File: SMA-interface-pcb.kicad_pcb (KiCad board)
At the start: 2 copper layers, 19 x 60 mm, 9 parts, among them J1 Conn_Coaxial, J3 Conn_01x02_Pin, J4 USB_A_Stacked, J5 Conn_01x02_Pin, Q1 AO3400A, U1 EL817

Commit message: updated schematic to v0
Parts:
- added D2: D_Schottky, Diode_SMD:D_3220_8050Metric_Pad2.65x5.15mm_HandSolder, F.Cu at (131.0, 100.3)
- added F2: Polyfuse, Fuse:fuse, F.Cu at (123.0, 85.5)
- added J2: Conn_Coaxial, Connector_Coaxial:SMA_Amphenol_901-143_Horizontal, F.Cu at (68.5, 63.5)
- added J6: Conn_Coaxial, Connector_Coaxial:SMA_Amphenol_901-143_Horizontal, F.Cu at (102.0, 63.5)
- added J7: Conn_Coaxial, Connector_Coaxial:SMA_Amphenol_901-143_Horizontal, F.Cu at (118.0, 63.5)
- added J8: USB_A_Stacked, Connector_USB:USB_A_Wuerth_61400826021_Horizontal_Stacked, F.Cu at (117.6, 120.0)
- added Q2: AO3400A, Package_TO_SOT_SMD:SOT-23, F.Cu at (74.0, 130.2)
- added Q3: AO3400A, Package_TO_SOT_SMD:SOT-23, F.Cu at (125.0, 142.0)
- added Q4: AO3400A, Package_TO_SOT_SMD:SOT-23, F.Cu at (73.9, 118.0)
- added Q5: AO3400A, Package_TO_SOT_SMD:SOT-23, F.Cu at (103.5, 143.5)
- added Q6: AO3400A, Package_TO_SOT_SMD:SOT-23, F.Cu at (124.5, 131.4)
- added Q7: AO3400A, Package_TO_SOT_SMD:SOT-23, F.Cu at (74.5, 143.5)
- added Q8: AO3400A, Package_TO_SOT_SMD:SOT-23, F.Cu at (73.9, 104.2)
- added R10: 10k, Resistor_THT:R_Axial_DIN0207_L6.3mm_D2.5mm_P2.54mm_Vertical, F.Cu at (65.5, 129.0)
- added R11: 100, Resistor_THT:R_Axial_DIN0207_L6.3mm_D2.5mm_P2.54mm_Vertical, F.Cu at (57.7, 119.1)
- added R12: 10k, Resistor_THT:R_Axial_DIN0207_L6.3mm_D2.5mm_P2.54mm_Vertical, F.Cu at (65.5, 117.0)
- added R13: 100, Resistor_THT:R_Axial_DIN0207_L6.3mm_D2.5mm_P2.54mm_Vertical, F.Cu at (95.0, 134.0)
- added R14: 10k, Resistor_THT:R_Axial_DIN0207_L6.3mm_D2.5mm_P2.54mm_Vertical, F.Cu at (95.0, 142.0)
- added R15: 100, Resistor_THT:R_Axial_DIN0207_L6.3mm_D2.5mm_P2.54mm_Vertical, F.Cu at (116.5, 130.5)
- added R16: 10k, Resistor_THT:R_Axial_DIN0207_L6.3mm_D2.5mm_P2.54mm_Vertical, F.Cu at (133.0, 132.5)
- added R17: 100, Resistor_THT:R_Axial_DIN0207_L6.3mm_D2.5mm_P2.54mm_Vertical, F.Cu at (57.9, 145.1)
- added R18: 10k, Resistor_THT:R_Axial_DIN0207_L6.3mm_D2.5mm_P2.54mm_Vertical, F.Cu at (66.0, 143.0)
- added R19: 100, Resistor_THT:R_Axial_DIN0207_L6.3mm_D2.5mm_P2.54mm_Vertical, F.Cu at (57.5, 105.1)
- added R2: R, Resistor_THT:R_Axial_DIN0207_L6.3mm_D2.5mm_P2.54mm_Vertical, F.Cu at (84.0, 73.7)
- added R20: 10k, Resistor_THT:R_Axial_DIN0207_L6.3mm_D2.5mm_P2.54mm_Vertical, F.Cu at (65.5, 103.1)
- added R4: R, Resistor_THT:R_Axial_DIN0207_L6.3mm_D2.5mm_P2.54mm_Vertical, F.Cu at (101.0, 73.5)
- added R6: R, Resistor_THT:R_Axial_DIN0207_L6.3mm_D2.5mm_P2.54mm_Vertical, F.Cu at (117.6, 72.9)
- added R7: 100, Resistor_THT:R_Axial_DIN0207_L6.3mm_D2.5mm_P2.54mm_Vertical, F.Cu at (56.9, 131.2)
- added R8: 100, Resistor_THT:R_Axial_DIN0207_L6.3mm_D2.5mm_P2.54mm_Vertical, F.Cu at (116.5, 143.0)
- added R9: 10k, Resistor_THT:R_Axial_DIN0207_L6.3mm_D2.5mm_P2.54mm_Vertical, F.Cu at (133.0, 142.5)
- added RZ1: RP2040-Zero, RP2040:RP2040_Zero_Castellated, F.Cu at (96.5, 116.0)
- J1: footprint SMA:SMA_Amphenol_901-143_Horizontal -> Connector_Coaxial:SMA_Amphenol_901-143_Horizontal
- J3: footprint SMA:Molex_Mini-Fit_Jr_5569-02A2_2x01_P4.20mm_Horizontal -> Connector_Molex:Molex_Mini-Fit_Jr_5569-02A2_2x01_P4.20mm_Horizontal
- Q1: moved to F.Cu
- R1: value R -> 100; footprint SMA:R_tht1270_smd3216 -> Resistor_THT:R_Axial_DIN0207_L6.3mm_D2.5mm_P2.54mm_Vertical
- R3: value R -> 10k; footprint SMA:R_tht1270_smd3216 -> Resistor_THT:R_Axial_DIN0207_L6.3mm_D2.5mm_P2.54mm_Vertical
- R5: footprint SMA:R_tht1270_smd3216 -> Resistor_THT:R_Axial_DIN0207_L6.3mm_D2.5mm_P2.54mm_Vertical
- U1: value EL817 -> 74HC14; footprint Package_DIP:DIP-4_W7.62mm_SMDSocket_SmallPads -> Button_Switch_SMD:SW_DIP_SPSTx07_Slide_KingTek_DSHP07TJ_W5.25mm_P1.27mm_JPin; moved to F.Cu
- moved J4 64.0 mm to (72.1, 86.5), turned to -90 degrees
- moved R5 61.5 mm to (68.0, 74.0), turned to 180 degrees
- moved R1 60.6 mm to (89.0, 134.0)
- moved R3 54.4 mm to (89.0, 142.0), turned to -90 degrees
- moved J1 45.5 mm to (85.0, 63.5)
- moved Q1 44.7 mm to (103.4, 134.9), turned to 0 degrees
- moved U1 37.4 mm to (96.5, 92.5), turned to 0 degrees
- moved J5 25.8 mm to (131.5, 60.0), turned to 90 degrees
- moved J3 8.24 mm to (132.5, 82.3)
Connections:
- J1 pad 1: Net-(J1-In) -> /sma1
- J3 pad 1: GND -> /power input
- J3 pad 2: VCC -> /vcc
- J4 pad 1: VCC -> /vcc
- J4 pad 2: unconnected-(J4-D1--Pad2) -> /2illumination1-
- J4 pad 3: /illumination -> /2sound1+
- J4 pad 5: VCC -> /vcc
- J4 pad 6: unconnected-(J4-D2--Pad6) -> /2illumination2-
- J4 pad 7: /illumination -> /2sound2+
- J5 pad 1: GND -> /power input
- J5 pad 2: VCC -> /vcc
- Q1 pad 3: /illumination -> Net-(J8-D2-)
- R1 pad 1: Net-(R1-Pad1) -> /illumination
- R5 pad 1: Net-(J1-In) -> /sma3
- R5 pad 2: Net-(R5-Pad2) -> GND
- U1 pad 1: Net-(R5-Pad2) -> /sma1
- U1 pad 2: GND -> /SMA_con1
- U1 pad 3: Net-(R1-Pad1) -> /sma2
- U1 pad 4: VCC -> /SMA_con2
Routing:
- net /vcc: track 0.00 -> 149.7 mm, vias 0 -> 6
- net /2sound1+: track 0.00 -> 75.1 mm, vias 0 -> 2
- net VCC: track 65.2 -> 0.00 mm
- net /2sound2+: track 0.00 -> 56.6 mm, vias 0 -> 2
- net /sma3: track 0.00 -> 44.7 mm
- net /2illumination2-: track 0.00 -> 42.1 mm, vias 0 -> 2
- net /sma4: track 0.00 -> 40.2 mm
- net Net-(RZ1-GP10): track 0.00 -> 37.9 mm
- net /sound: track 0.00 -> 33.6 mm, vias 0 -> 2
- net /SMA_con4: track 0.00 -> 33.3 mm, vias 0 -> 2
- net Net-(J8-D1-): track 0.00 -> 33.0 mm, vias 0 -> 2
- net /sma2: track 0.00 -> 32.2 mm
- net /power input: track 0.00 -> 31.7 mm
- net Net-(R5-Pad2): track 30.3 -> 0.00 mm
- net /sound2: track 0.00 -> 30.2 mm
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- added copper zone on F.Cu, net GND
- removed copper zone on B.Cu, net GND
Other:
- board size 19 x 60 mm -> 15.6 x 20.9 mm

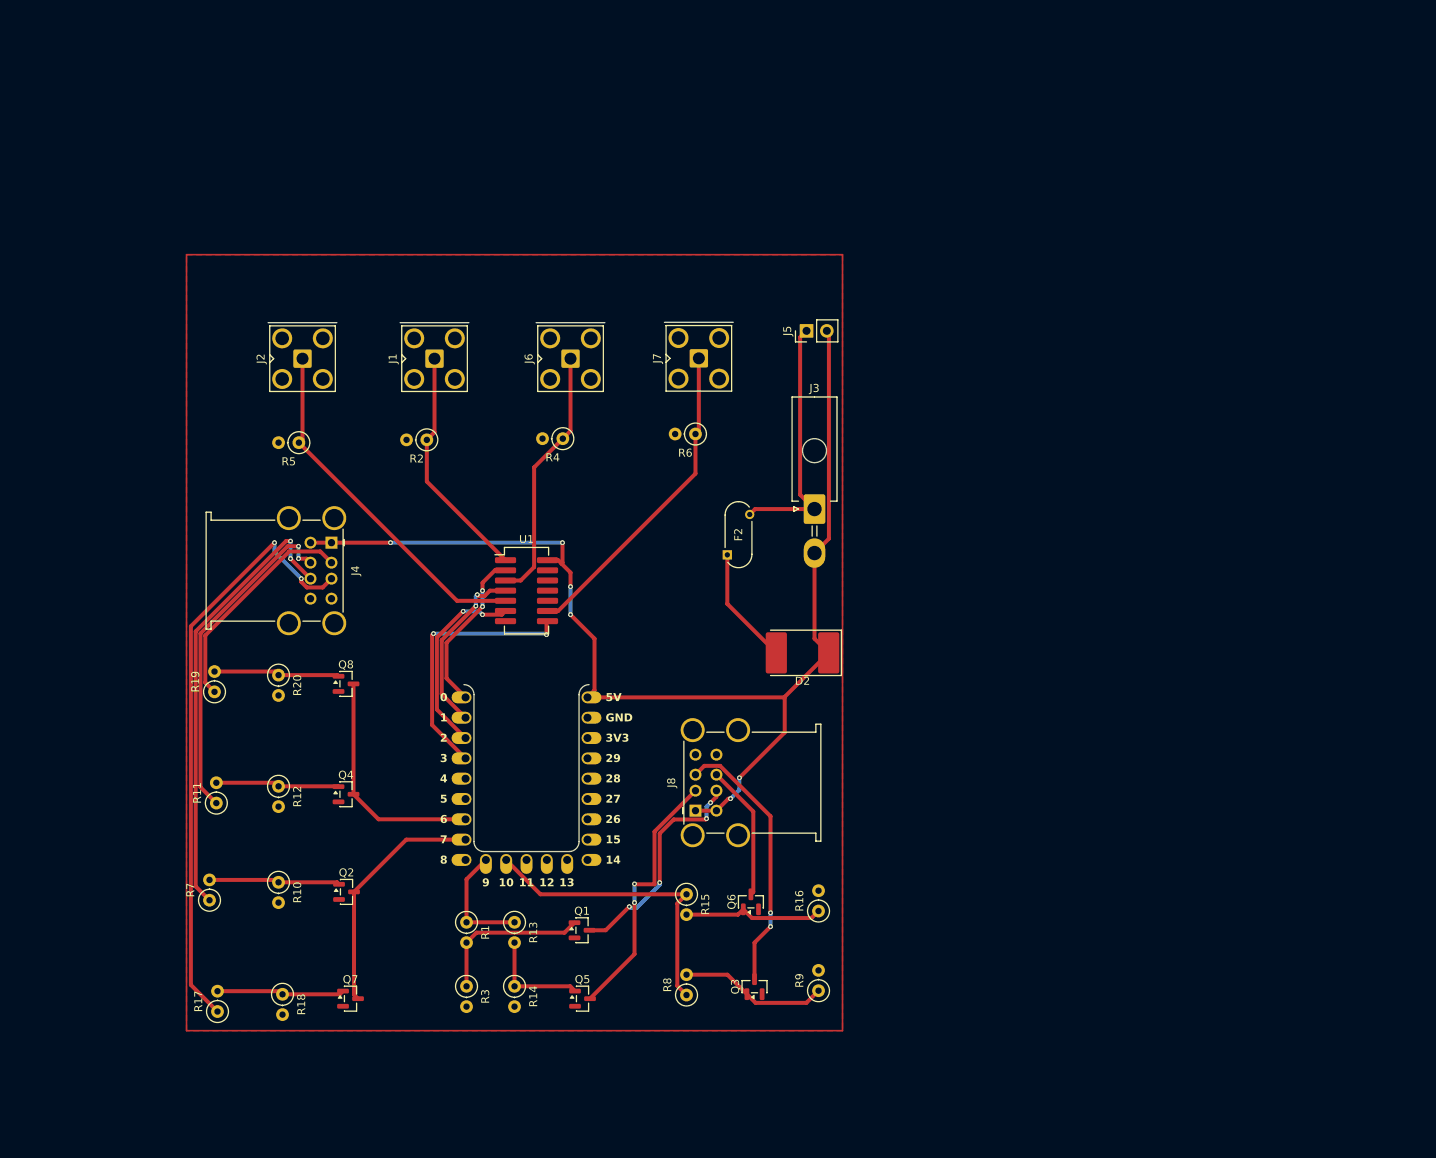
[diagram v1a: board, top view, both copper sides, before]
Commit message: updated schematic with appropriate symbols, to be verified
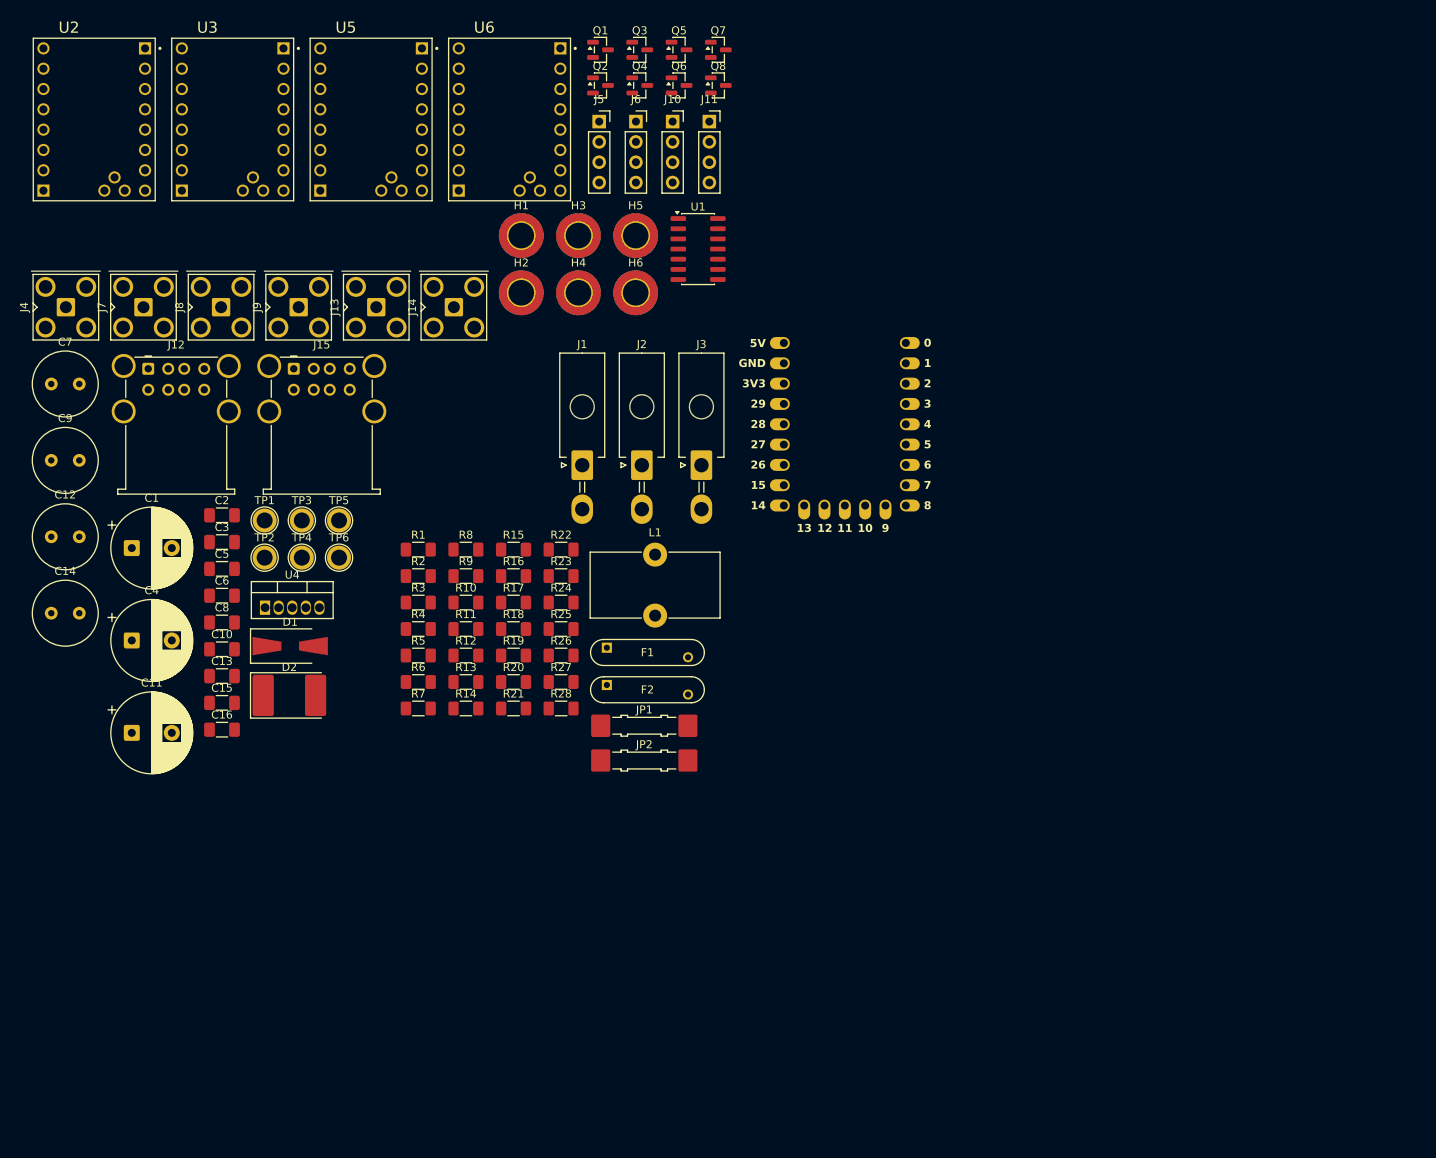
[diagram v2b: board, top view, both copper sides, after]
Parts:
- added C1: 470µF 50V, Capacitor_THT:CP_Radial_D10.0mm_P5.00mm, F.Cu at (47.2, 87.2)
- added C10: 100nF 50V, Capacitor_SMD:C_1206_3216Metric_Pad1.33x1.80mm_HandSolder, F.Cu at (58.4, 99.8)
- added C11: 470µF 50V, Capacitor_THT:CP_Radial_D10.0mm_P5.00mm, F.Cu at (47.2, 110.3)
- added C12: 100µF 50V, Capacitor_THT:C_Radial_D8.0mm_H11.5mm_P3.50mm, F.Cu at (37.1, 85.8)
- added C13: 100nF 50V, Capacitor_SMD:C_1206_3216Metric_Pad1.33x1.80mm_HandSolder, F.Cu at (58.4, 103.2)
- added C14: 100µF 50V, Capacitor_THT:C_Radial_D8.0mm_H11.5mm_P3.50mm, F.Cu at (37.1, 95.3)
- added C15: 100nF 50V, Capacitor_SMD:C_1206_3216Metric_Pad1.33x1.80mm_HandSolder, F.Cu at (58.4, 106.5)
- added C16: 100nF 16V, Capacitor_SMD:C_1206_3216Metric_Pad1.33x1.80mm_HandSolder, F.Cu at (58.4, 109.9)
- added C2: 1µF 50V, Capacitor_SMD:C_1206_3216Metric_Pad1.33x1.80mm_HandSolder, F.Cu at (58.4, 83.1)
- added C3: 100nF 50V, Capacitor_SMD:C_1206_3216Metric_Pad1.33x1.80mm_HandSolder, F.Cu at (58.4, 86.4)
- added C4: 470µF 16V, Capacitor_THT:CP_Radial_D10.0mm_P5.00mm, F.Cu at (47.2, 98.7)
- added C5: 1µF 16V, Capacitor_SMD:C_1206_3216Metric_Pad1.33x1.80mm_HandSolder, F.Cu at (58.4, 89.8)
- added C6: 100nF 16V, Capacitor_SMD:C_1206_3216Metric_Pad1.33x1.80mm_HandSolder, F.Cu at (58.4, 93.1)
- added C7: 100µF 50V, Capacitor_THT:C_Radial_D8.0mm_H11.5mm_P3.50mm, F.Cu at (37.1, 66.7)
- added C8: 100nF 50V, Capacitor_SMD:C_1206_3216Metric_Pad1.33x1.80mm_HandSolder, F.Cu at (58.4, 96.5)
- added C9: 100µF 50V, Capacitor_THT:C_Radial_D8.0mm_H11.5mm_P3.50mm, F.Cu at (37.1, 76.2)
- added D1: D_TVS, Diode_SMD:D_SMA-SMB_Universal_Handsoldering, F.Cu at (67.0, 99.4)
- added F1: RUEF500, NeuroACT:FUSE_RUEF500_LTF, F.Cu at (111.6, 100.2)
- added H1: MountingHole, MountingHole:MountingHole_3.2mm_M3_DIN965_Pad_TopBottom, F.Cu at (95.8, 48.1)
- added H2: MountingHole, MountingHole:MountingHole_3.2mm_M3_DIN965_Pad_TopBottom, F.Cu at (95.8, 55.3)
- added H3: MountingHole, MountingHole:MountingHole_3.2mm_M3_DIN965_Pad_TopBottom, F.Cu at (103.0, 48.1)
- added H4: MountingHole, MountingHole:MountingHole_3.2mm_M3_DIN965_Pad_TopBottom, F.Cu at (103.0, 55.3)
- added H5: MountingHole, MountingHole:MountingHole_3.2mm_M3_DIN965_Pad_TopBottom, F.Cu at (110.1, 48.1)
- added H6: MountingHole, MountingHole:MountingHole_3.2mm_M3_DIN965_Pad_TopBottom, F.Cu at (110.1, 55.3)
- added J10: Conn_01x04_Pin, Connector_PinSocket_2.54mm:PinSocket_1x04_P2.54mm_Vertical, F.Cu at (114.8, 33.9)
- added J11: Conn_01x04_Pin, Connector_PinSocket_2.54mm:PinSocket_1x04_P2.54mm_Vertical, F.Cu at (119.4, 33.9)
- added J12: USB_A_Stacked, Connector_USB:USB_A_Wuerth_61400826021_Horizontal_Stacked, F.Cu at (49.2, 64.8)
- added J13: Conn_Coaxial, Connector_Coaxial:SMA_Amphenol_901-143_Horizontal, F.Cu at (77.7, 57.1)
- added J14: Conn_Coaxial, Connector_Coaxial:SMA_Amphenol_901-143_Horizontal, F.Cu at (87.4, 57.1)
- added J15: USB_A_Stacked, Connector_USB:USB_A_Wuerth_61400826021_Horizontal_Stacked, F.Cu at (67.4, 64.8)
- added J9: Conn_Coaxial, Connector_Coaxial:SMA_Amphenol_901-143_Horizontal, F.Cu at (68.0, 57.1)
- added JP1: Jumper_3_Open, Jumper:Jumper_Harwin_S1621_P10.9mm, F.Cu at (111.2, 109.4)
- added JP2: Jumper_3_Open, Jumper:Jumper_Harwin_S1621_P10.9mm, F.Cu at (111.2, 113.7)
- added L1: 33uH, Inductor_THT:L_Toroid_Vertical_L16.0mm_W8.0mm_P7.62mm, F.Cu at (112.6, 88.0)
- added R21: 10k, Resistor_SMD:R_1206_3216Metric_Pad1.30x1.75mm_HandSolder, F.Cu at (94.9, 107.2)
- added R22: 10 kΩ, Resistor_SMD:R_1206_3216Metric_Pad1.30x1.75mm_HandSolder, F.Cu at (100.8, 87.4)
- added R23: 10 kΩ, Resistor_SMD:R_1206_3216Metric_Pad1.30x1.75mm_HandSolder, F.Cu at (100.8, 90.7)
- added R24: 10k, Resistor_SMD:R_1206_3216Metric_Pad1.30x1.75mm_HandSolder, F.Cu at (100.8, 94.0)
- added R25: 10k, Resistor_SMD:R_1206_3216Metric_Pad1.30x1.75mm_HandSolder, F.Cu at (100.8, 97.3)
- added R26: 10 kΩ, Resistor_SMD:R_1206_3216Metric_Pad1.30x1.75mm_HandSolder, F.Cu at (100.8, 100.6)
- added R27: 10 kΩ, Resistor_SMD:R_1206_3216Metric_Pad1.30x1.75mm_HandSolder, F.Cu at (100.8, 103.9)
- added R28: 0 ohm, Resistor_SMD:R_1206_3216Metric_Pad1.30x1.75mm_HandSolder, F.Cu at (100.8, 107.2)
- added TP1: TestPoint, TestPoint:TestPoint_Plated_Hole_D2.0mm, F.Cu at (63.8, 83.7)
- added TP2: TestPoint, TestPoint:TestPoint_Plated_Hole_D2.0mm, F.Cu at (63.8, 88.4)
- added TP3: TestPoint, TestPoint:TestPoint_Plated_Hole_D2.0mm, F.Cu at (68.4, 83.7)
- added TP4: TestPoint, TestPoint:TestPoint_Plated_Hole_D2.0mm, F.Cu at (68.4, 88.4)
- added TP5: TestPoint, TestPoint:TestPoint_Plated_Hole_D2.0mm, F.Cu at (73.1, 83.7)
- added TP6: TestPoint, TestPoint:TestPoint_Plated_Hole_D2.0mm, F.Cu at (73.1, 88.4)
- added U2: TMC2209_SILENTSTEPSTICK, NeuroACT:MODULE_TMC2208_SILENTSTEPSTICK, F.Cu at (42.5, 33.6)
- added U3: TMC2209_SILENTSTEPSTICK, NeuroACT:MODULE_TMC2208_SILENTSTEPSTICK, F.Cu at (59.8, 33.6)
- added U4: LM2596T-5, Package_TO_SOT_THT:TO-220-5_Vertical, F.Cu at (63.8, 94.6)
- added U5: TMC2209_SILENTSTEPSTICK, NeuroACT:MODULE_TMC2208_SILENTSTEPSTICK, F.Cu at (77.1, 33.6)
- added U6: TMC2209_SILENTSTEPSTICK, NeuroACT:MODULE_TMC2208_SILENTSTEPSTICK, F.Cu at (94.4, 33.6)
- D2: value D_Schottky -> SS56B
- F2: value Polyfuse -> RUEF500; footprint Fuse:fuse -> NeuroACT:FUSE_RUEF500_LTF
- J1, J2: value Conn_Coaxial -> Conn_01x02_Pin; footprint Connector_Coaxial:SMA_Amphenol_901-143_Horizontal -> Connector_Molex:Molex_Mini-Fit_Jr_5569-02A2_2x01_P4.20mm_Horizontal
- J4, J8: value USB_A_Stacked -> Conn_Coaxial; footprint Connector_USB:USB_A_Wuerth_61400826021_Horizontal_Stacked -> Connector_Coaxial:SMA_Amphenol_901-143_Horizontal
- J5: value Conn_01x02_Pin -> Conn_01x04_Pin; footprint Connector_PinHeader_2.54mm:PinHeader_1x02_P2.54mm_Vertical -> Connector_PinSocket_2.54mm:PinSocket_1x04_P2.54mm_Vertical
- J6: value Conn_Coaxial -> Conn_01x04_Pin; footprint Connector_Coaxial:SMA_Amphenol_901-143_Horizontal -> Connector_PinSocket_2.54mm:PinSocket_1x04_P2.54mm_Vertical
- R1, R11, R14, R16, R18, R20: footprint Resistor_THT:R_Axial_DIN0207_L6.3mm_D2.5mm_P2.54mm_Vertical -> Resistor_SMD:R_1206_3216Metric_Pad1.30x1.75mm_HandSolder
- R10, R12, R3, R9: value 10k -> 100; footprint Resistor_THT:R_Axial_DIN0207_L6.3mm_D2.5mm_P2.54mm_Vertical -> Resistor_SMD:R_1206_3216Metric_Pad1.30x1.75mm_HandSolder
- R13, R15, R7, R8: value 100 -> 10k; footprint Resistor_THT:R_Axial_DIN0207_L6.3mm_D2.5mm_P2.54mm_Vertical -> Resistor_SMD:R_1206_3216Metric_Pad1.30x1.75mm_HandSolder
- R17, R19: value 100 -> 10 kΩ; footprint Resistor_THT:R_Axial_DIN0207_L6.3mm_D2.5mm_P2.54mm_Vertical -> Resistor_SMD:R_1206_3216Metric_Pad1.30x1.75mm_HandSolder
- R2, R4: value R -> 100; footprint Resistor_THT:R_Axial_DIN0207_L6.3mm_D2.5mm_P2.54mm_Vertical -> Resistor_SMD:R_1206_3216Metric_Pad1.30x1.75mm_HandSolder
- R5, R6: value R -> 10k; footprint Resistor_THT:R_Axial_DIN0207_L6.3mm_D2.5mm_P2.54mm_Vertical -> Resistor_SMD:R_1206_3216Metric_Pad1.30x1.75mm_HandSolder
- RZ1: footprint RP2040:RP2040_Zero_Castellated -> NeuroACT:RP2040_Zero
- U1: value 74HC14 -> 74HC7014; footprint Button_Switch_SMD:SW_DIP_SPSTx07_Slide_KingTek_DSHP07TJ_W5.25mm_P1.27mm_JPin -> Package_SO:SOIC-14_3.9x8.7mm_P1.27mm
- moved Q7 127.2 mm to (120.5, 24.9)
- moved Q5 119.2 mm to (115.6, 24.9)
- moved Q3 118.0 mm to (110.7, 24.9), turned to 0 degrees
- moved Q1 110.1 mm to (105.7, 24.9)
- moved Q2 105.7 mm to (105.7, 29.3)
- moved Q6 102.4 mm to (115.6, 29.3), turned to 0 degrees
- moved Q4 95.9 mm to (110.7, 29.3)
- moved Q8 88.1 mm to (120.5, 29.3)
- moved J8 86.5 mm to (58.3, 57.1), turned to 0 degrees
- moved J7 69.7 mm to (48.6, 57.1)
- moved R9 68.0 mm to (88.9, 90.7), turned to 0 degrees
- moved D2 64.4 mm to (66.9, 105.6), turned to 0 degrees
- moved R17 63.1 mm to (94.9, 94.0), turned to 0 degrees
- moved R8 62.1 mm to (88.9, 87.4), turned to 0 degrees
- moved RZ1 59.5 mm to (136.3, 71.7)
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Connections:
- D2 pad 1: /vcc -> Net-(D2-K)
- D2 pad 2: Net-(D2-A) -> GND
- F2 pad 1: Net-(D2-A) -> /24V_input
- F2 pad 2: /power input -> /24V_motor
- J1 pad 1: /sma1 -> /24V_input
- J2 pad 1: /sma3 -> /24V_input
- J3 pad 1: /power input -> /5V_main
- J3 pad 2: /vcc -> GND
- J4 pad 1: /vcc -> Net-(J4-In)
- J4 pad 2: /2illumination1- -> GND
- J5 pad 1: /power input -> Net-(J5-Pin_1)
- J5 pad 2: /vcc -> Net-(J5-Pin_2)
- J6 pad 1: /sma2 -> Net-(J6-Pin_1)
- J6 pad 2: GND -> Net-(J6-Pin_2)
- J7 pad 1: /sma4 -> Net-(J7-In)
- J8 pad 1: /vcc -> Net-(J8-In)
- J8 pad 2: Net-(J8-D1-) -> GND
- Q1 pad 3: Net-(J8-D2-) -> /illumination_A
- Q2 pad 3: /sound2 -> /illumination_B
- Q3 pad 3: /sound -> /sound_A
- Q4 pad 3: /illumination2 -> /sound_B
- Q5 pad 3: Net-(J8-D1-) -> /illumination_C
- Q6 pad 3: /sound2+ -> /illumination_D
- Q7 pad 3: /sound2 -> /sound_C
- Q8 pad 3: /illumination2 -> /sound_D
- R1 pad 1: /illumination -> /Dout_light_A
- R10 pad 1: Net-(Q2-G) -> /Dout_light_D
- R10 pad 2: GND -> Net-(Q6-G)
- R11 pad 1: /2illumination2- -> /Dout_sound_C
- R11 pad 2: Net-(Q4-G) -> Net-(Q7-G)
- R12 pad 1: Net-(Q4-G) -> /Dout_sound_D
- R12 pad 2: GND -> Net-(Q8-G)
- R13 pad 1: /illumination -> Net-(Q5-G)
- R13 pad 2: Net-(Q5-G) -> GND
- R14 pad 1: Net-(Q5-G) -> Net-(Q6-G)
- R15 pad 1: Net-(RZ1-GP10) -> Net-(Q7-G)
- R15 pad 2: Net-(Q6-G) -> GND
- R16 pad 1: Net-(Q6-G) -> Net-(Q8-G)
- R17 pad 1: /2sound1+ -> Net-(J4-In)
- R17 pad 2: Net-(Q7-G) -> GND
- R18 pad 1: Net-(Q7-G) -> /Enable
- R18 pad 2: GND -> /3.3V
- R19 pad 1: /2illumination1- -> Net-(J7-In)
- R19 pad 2: Net-(Q8-G) -> GND
- R2 pad 1: /sma1 -> /Dout_light_B
- R2 pad 2: GND -> Net-(Q2-G)
- R20 pad 1: Net-(Q8-G) -> GND
- R20 pad 2: GND -> Net-(U2-SPRD)
- R3 pad 1: Net-(Q1-G) -> /Dout_sound_A
- R3 pad 2: GND -> Net-(Q3-G)
- R4 pad 1: /sma2 -> /Dout_sound_B
- R4 pad 2: GND -> Net-(Q4-G)
- R5 pad 1: /sma3 -> Net-(Q1-G)
- R6 pad 1: /sma4 -> Net-(Q2-G)
- R7 pad 1: /2sound2+ -> Net-(Q3-G)
- R7 pad 2: Net-(Q2-G) -> GND
- R8 pad 1: Net-(RZ1-GP10) -> Net-(Q4-G)
- R8 pad 2: Net-(Q3-G) -> GND
- R9 pad 1: Net-(Q3-G) -> /Dout_light_C
- R9 pad 2: GND -> Net-(Q5-G)
- RZ1 pad 1: /SMA_con1 -> /Enable
- RZ1 pad 10: /illumination -> /Dout_light_B
- RZ1 pad 11: Net-(RZ1-GP10) -> /Dout_light_C
- RZ1 pad 12: unconnected-(RZ1-GP11-Pad12) -> /Dout_light_D
- RZ1 pad 13: unconnected-(RZ1-GP12-Pad13) -> /Dout_sound_A
- RZ1 pad 14: unconnected-(RZ1-GP13-Pad14) -> /Dout_sound_B
- RZ1 pad 15: unconnected-(RZ1-GP14-Pad15) -> /Dout_sound_C
- RZ1 pad 16: unconnected-(RZ1-GP15-Pad16) -> /Dout_sound_D
- RZ1 pad 17: unconnected-(RZ1-GP26-Pad17) -> /mot_step_D
- RZ1 pad 18: unconnected-(RZ1-GP27-Pad18) -> /mot_step_C
- RZ1 pad 19: unconnected-(RZ1-GP28-Pad19) -> /mot_step_B
- RZ1 pad 2: /SMA_con2 -> /Direction
- RZ1 pad 20: unconnected-(RZ1-GP29-Pad20) -> /mot_step_A
- RZ1 pad 21: unconnected-(RZ1-3V3-Pad21) -> /3.3V
- RZ1 pad 23: /vcc -> /5V_main
- RZ1 pad 3: /SMA_con3 -> /SMA_con1
- RZ1 pad 4: /SMA_con4 -> /SMA_con2
- RZ1 pad 5: unconnected-(RZ1-GP4-Pad5) -> /SMA_con3
- RZ1 pad 6: unconnected-(RZ1-GP5-Pad6) -> /SMA_con4
- RZ1 pad 7: /illumination2 -> /SMA_con5
- RZ1 pad 8: /sound2 -> /SMA_con6
- RZ1 pad 9: unconnected-(RZ1-GP8-Pad9) -> /Dout_light_A
- U1 pad 1: /sma1 -> Net-(J4-In)
- U1 pad 10: (no net) -> /SMA_con5
- U1 pad 11: (no net) -> Net-(J13-In)
- U1 pad 12: (no net) -> /SMA_con6
- U1 pad 13: (no net) -> Net-(J14-In)
- U1 pad 14: /vcc -> /3.3V
- U1 pad 3: /sma2 -> Net-(J7-In)
- U1 pad 5: /sma3 -> Net-(J8-In)
- U1 pad 9: /sma4 -> Net-(J9-In)
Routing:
- net /vcc: track 149.7 -> 0.00 mm, vias 6 -> 0
- net /2sound1+: track 75.1 -> 0.00 mm, vias 2 -> 0
- net /2sound2+: track 56.6 -> 0.00 mm, vias 2 -> 0
- net /sma3: track 44.7 -> 0.00 mm
- net /2illumination2-: track 42.1 -> 0.00 mm, vias 2 -> 0
- net /sma4: track 40.2 -> 0.00 mm
- net Net-(RZ1-GP10): track 37.9 -> 0.00 mm
- net /sound: track 33.6 -> 0.00 mm, vias 2 -> 0
- net /SMA_con4: track 33.3 -> 0.00 mm, vias 2 -> 0
- net Net-(J8-D1-): track 33.0 -> 0.00 mm, vias 2 -> 0
- net /sma2: track 32.2 -> 0.00 mm
- net /power input: track 31.7 -> 0.00 mm
- net /sound2: track 30.2 -> 0.00 mm
- net /sma1: track 29.7 -> 0.00 mm
- net /illumination2: track 29.1 -> 0.00 mm
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- removed copper zone on F.Cu, net GND
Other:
- board outline removed
